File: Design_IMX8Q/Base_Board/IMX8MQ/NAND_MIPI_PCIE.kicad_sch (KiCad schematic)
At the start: 6 parts, among them U1 MIMX8MQ6CVAHZAB, U7 MT25QUxxxxxx1xW7, X1 ABLNO

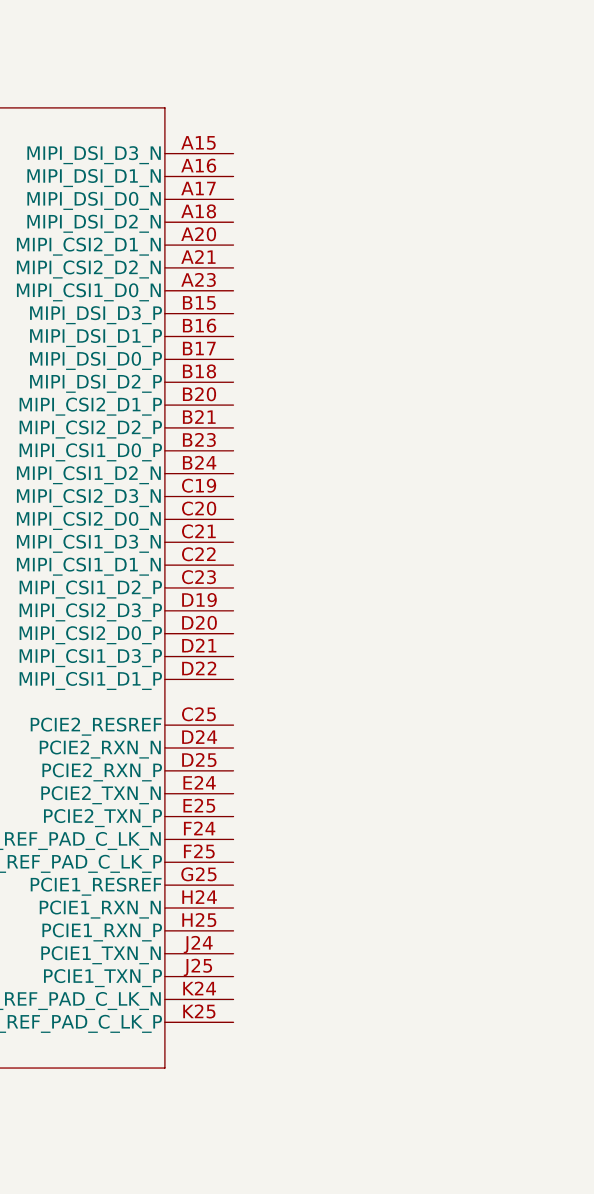
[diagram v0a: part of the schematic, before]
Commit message: Update IMX6QP and IMX8MQ
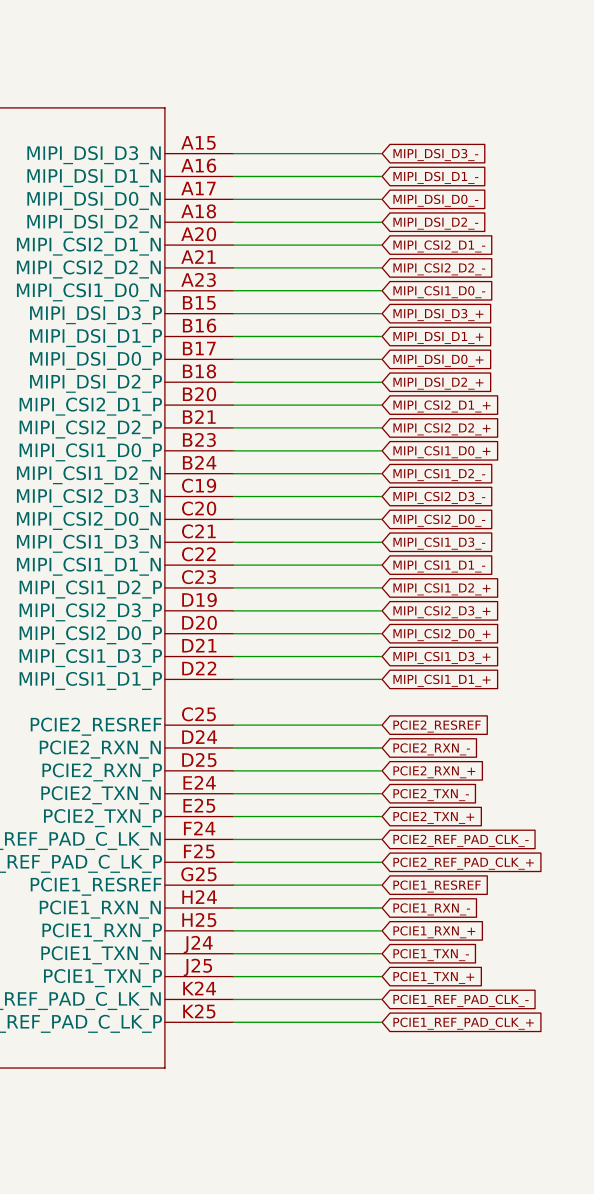
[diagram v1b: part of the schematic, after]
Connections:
- net MIPI_DSI_D3_-: now reaches U1.A15 (MIPI_DSI_D3_N)
- net MIPI_DSI_D1_-: now reaches U1.A16 (MIPI_DSI_D1_N)
- net MIPI_DSI_D0_-: now reaches U1.A17 (MIPI_DSI_D0_N)
- net MIPI_DSI_D2_-: now reaches U1.A18 (MIPI_DSI_D2_N)
- net MIPI_CSI2_D1_-: now reaches U1.A20 (MIPI_CSI2_D1_N)
- net MIPI_CSI2_D2_-: now reaches U1.A21 (MIPI_CSI2_D2_N)
- net MIPI_CSI1_D0_-: now reaches U1.A23 (MIPI_CSI1_D0_N)
- net MIPI_DSI_D3_+: now reaches U1.B15 (MIPI_DSI_D3_P)
- net MIPI_DSI_D1_+: now reaches U1.B16 (MIPI_DSI_D1_P)
- net MIPI_DSI_D0_+: now reaches U1.B17 (MIPI_DSI_D0_P)
- net MIPI_DSI_D2_+: now reaches U1.B18 (MIPI_DSI_D2_P)
- net MIPI_CSI2_D1_+: now reaches U1.B20 (MIPI_CSI2_D1_P)
- net MIPI_CSI2_D2_+: now reaches U1.B21 (MIPI_CSI2_D2_P)
- net MIPI_CSI1_D0_+: now reaches U1.B23 (MIPI_CSI1_D0_P)
- net MIPI_CSI1_D2_-: now reaches U1.B24 (MIPI_CSI1_D2_N)
- net MIPI_CSI2_D3_-: now reaches U1.C19 (MIPI_CSI2_D3_N)
- net MIPI_CSI2_D0_-: now reaches U1.C20 (MIPI_CSI2_D0_N)
- net MIPI_CSI1_D3_-: now reaches U1.C21 (MIPI_CSI1_D3_N)
- net MIPI_CSI1_D1_-: now reaches U1.C22 (MIPI_CSI1_D1_N)
- net MIPI_CSI1_D2_+: now reaches U1.C23 (MIPI_CSI1_D2_P)
- net PCIE2_RESREF: now reaches U1.C25 (PCIE2_RESREF)
- net MIPI_CSI2_D3_+: now reaches U1.D19 (MIPI_CSI2_D3_P)
- net MIPI_CSI2_D0_+: now reaches U1.D20 (MIPI_CSI2_D0_P)
- net MIPI_CSI1_D3_+: now reaches U1.D21 (MIPI_CSI1_D3_P)
- net MIPI_CSI1_D1_+: now reaches U1.D22 (MIPI_CSI1_D1_P)
- net PCIE2_RXN_-: now reaches U1.D24 (PCIE2_RXN_N)
- net PCIE2_RXN_+: now reaches U1.D25 (PCIE2_RXN_P)
- net PCIE2_TXN_-: now reaches U1.E24 (PCIE2_TXN_N)
- net PCIE2_TXN_+: now reaches U1.E25 (PCIE2_TXN_P)
- net PCIE2_REF_PAD_CLK_-: now reaches U1.F24 (PCIE2_REF_PAD_C_LK_N)
- net PCIE2_REF_PAD_CLK_+: now reaches U1.F25 (PCIE2_REF_PAD_C_LK_P)
- net PCIE1_RESREF: now reaches U1.G25 (PCIE1_RESREF)
- net PCIE1_RXN_-: now reaches U1.H24 (PCIE1_RXN_N)
- net PCIE1_RXN_+: now reaches U1.H25 (PCIE1_RXN_P)
- net PCIE1_TXN_-: now reaches U1.J24 (PCIE1_TXN_N)
- net PCIE1_TXN_+: now reaches U1.J25 (PCIE1_TXN_P)
- net PCIE1_REF_PAD_CLK_-: now reaches U1.K24 (PCIE1_REF_PAD_C_LK_N)
- net PCIE1_REF_PAD_CLK_+: now reaches U1.K25 (PCIE1_REF_PAD_C_LK_P)

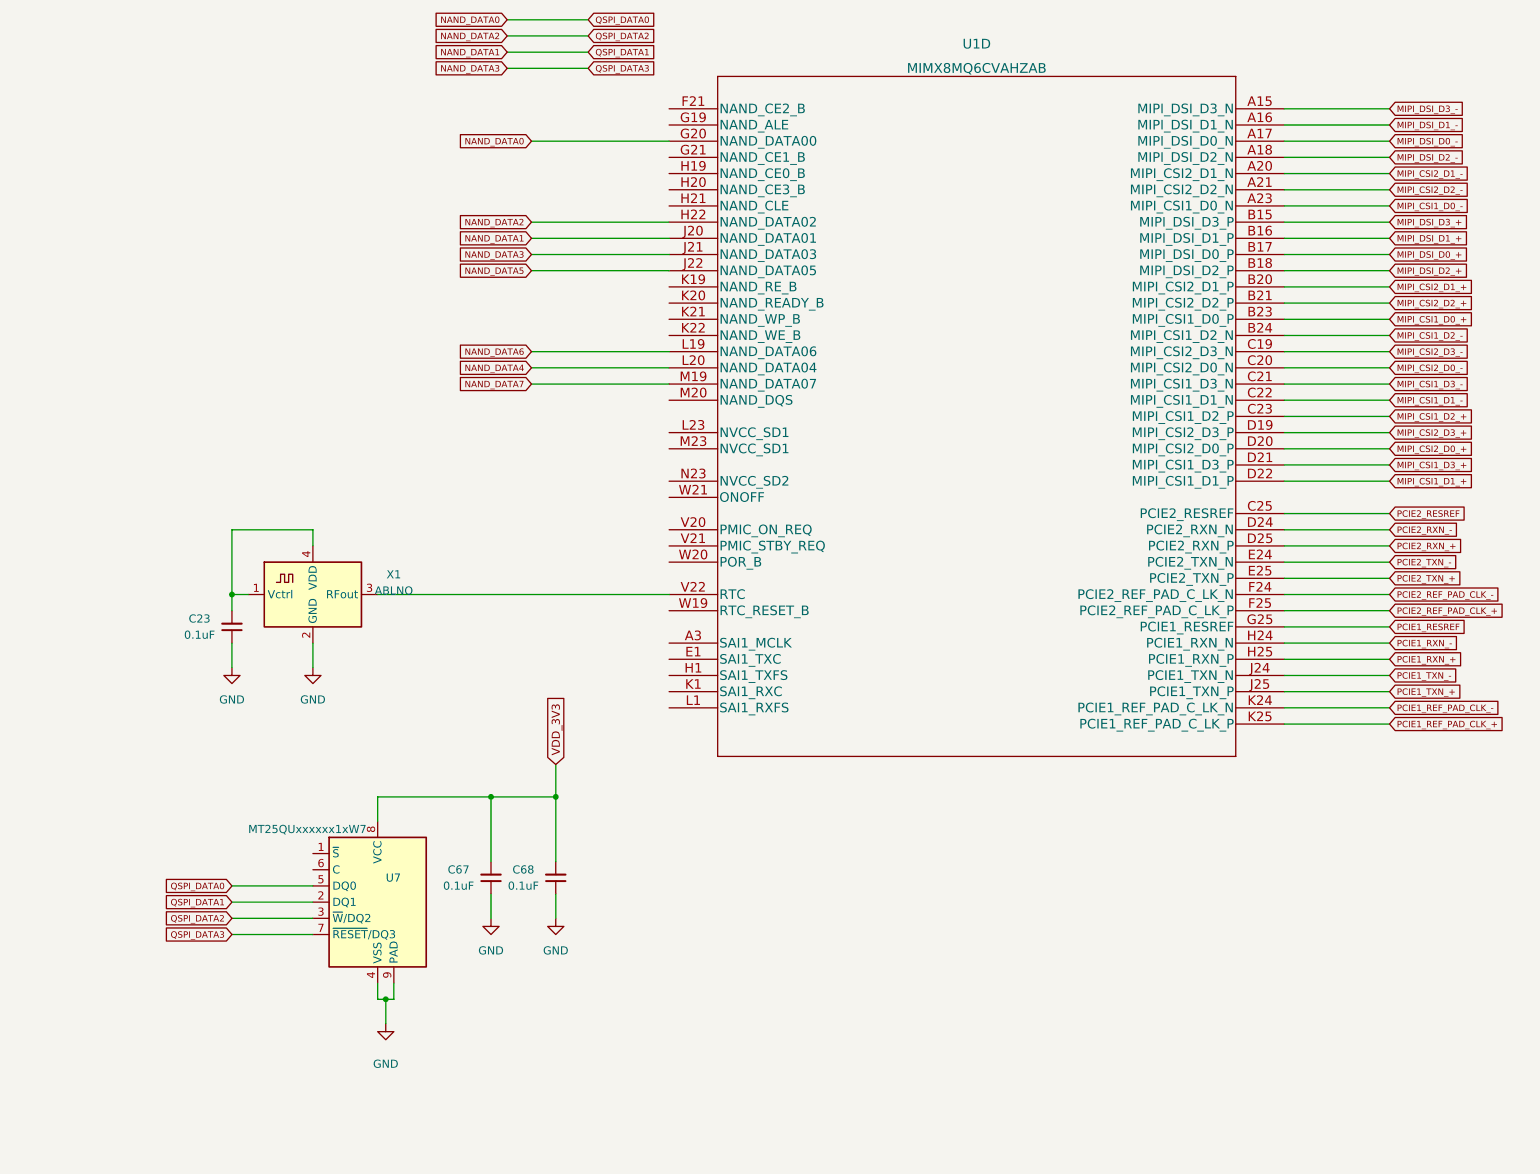
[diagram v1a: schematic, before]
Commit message: Add QSPI and more color
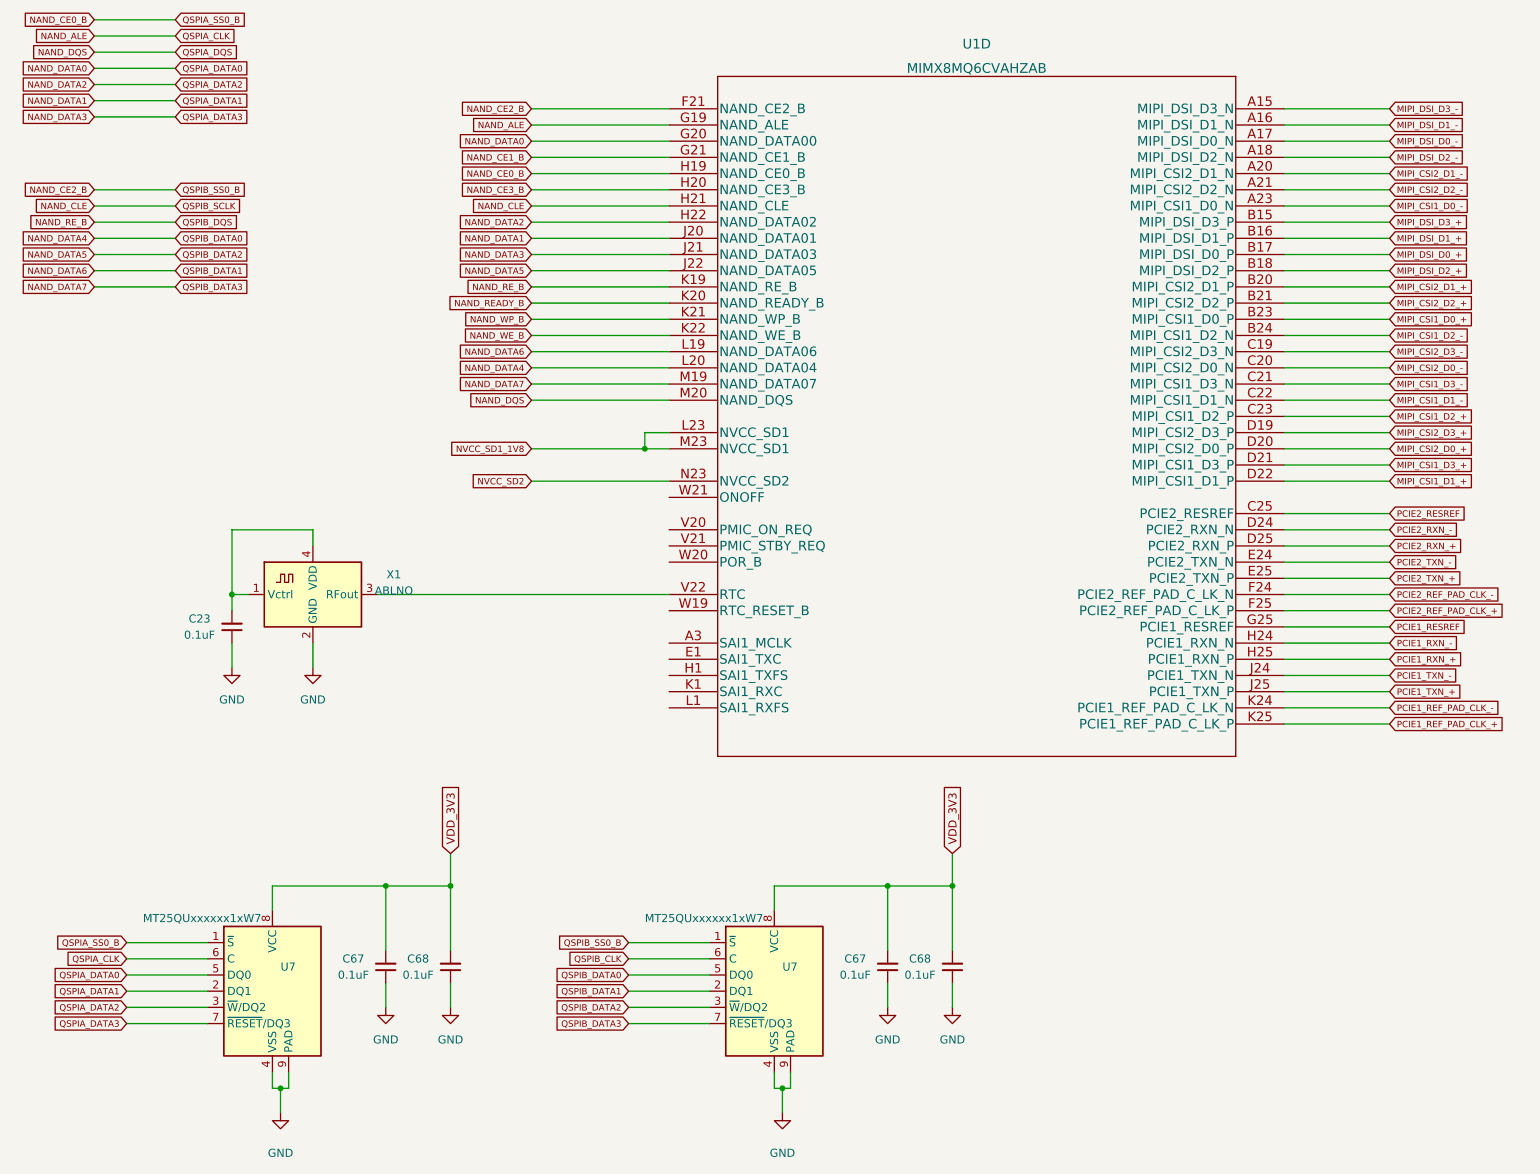
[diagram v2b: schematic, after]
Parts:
- added C67, C68: 0.1uF, Capacitor_SMD:C_0402_1005Metric, symbol Device:C_Small
- added U7: MT25QUxxxxxx1xW7, Package_DFN_QFN:W-PDFN-8-1EP_6x5mm_P1.27mm_EP3x3mm, symbol Memory_Flash:MT25QUxxxxxx1xW7
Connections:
- net GND: now also C67.1, C68.1, U7.4 (VSS), U7.9 (PAD)
- net NAND_DATA4: now also U7.5 (DQ0)
- net NAND_DATA5: now also U7.3 (~{W}/DQ2)
- net NAND_DATA6: now also U7.2 (DQ1)
- net NAND_DATA7: now also U7.7 (~{RESET}/DQ3)
- net VDD_3V3: now also C67.2, C68.2, U7.8 (VCC)
- net NAND_CE0_B: now reaches U7.1 (~{S})
- net NAND_CE0_B: now also U1.H19 (NAND_CE0_B)
- net NAND_ALE: now reaches U7.6 (C)
- net NAND_ALE: now also U1.G19 (NAND_ALE)
- net NAND_CE2_B: now reaches U1.F21 (NAND_CE2_B)
- net NAND_CE2_B: now also U7.1 (~{S})
- net NAND_CE1_B: now reaches U1.G21 (NAND_CE1_B)
- net NAND_CE3_B: now reaches U1.H20 (NAND_CE3_B)
- net NAND_CLE: now reaches U1.H21 (NAND_CLE)
- net NAND_RE_B: now reaches U1.K19 (NAND_RE_B)
- net NAND_READY_B: now reaches U1.K20 (NAND_READY_B)
- net NAND_WP_B: now reaches U1.K21 (NAND_WP_B)
- net NAND_WE_B: now reaches U1.K22 (NAND_WE_B)
- net NVCC_SD1_1V8: now reaches U1.L23 (NVCC_SD1)
- net NVCC_SD1_1V8: now also U1.M23 (NVCC_SD1)
- net NAND_DQS: now reaches U1.M20 (NAND_DQS)
- net NVCC_SD2: now reaches U1.N23 (NVCC_SD2)
- new net QSPIB_CLK: U7.6 (C)
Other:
- moved on the sheet: C67, C68, U7

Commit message: it was inserted power control system
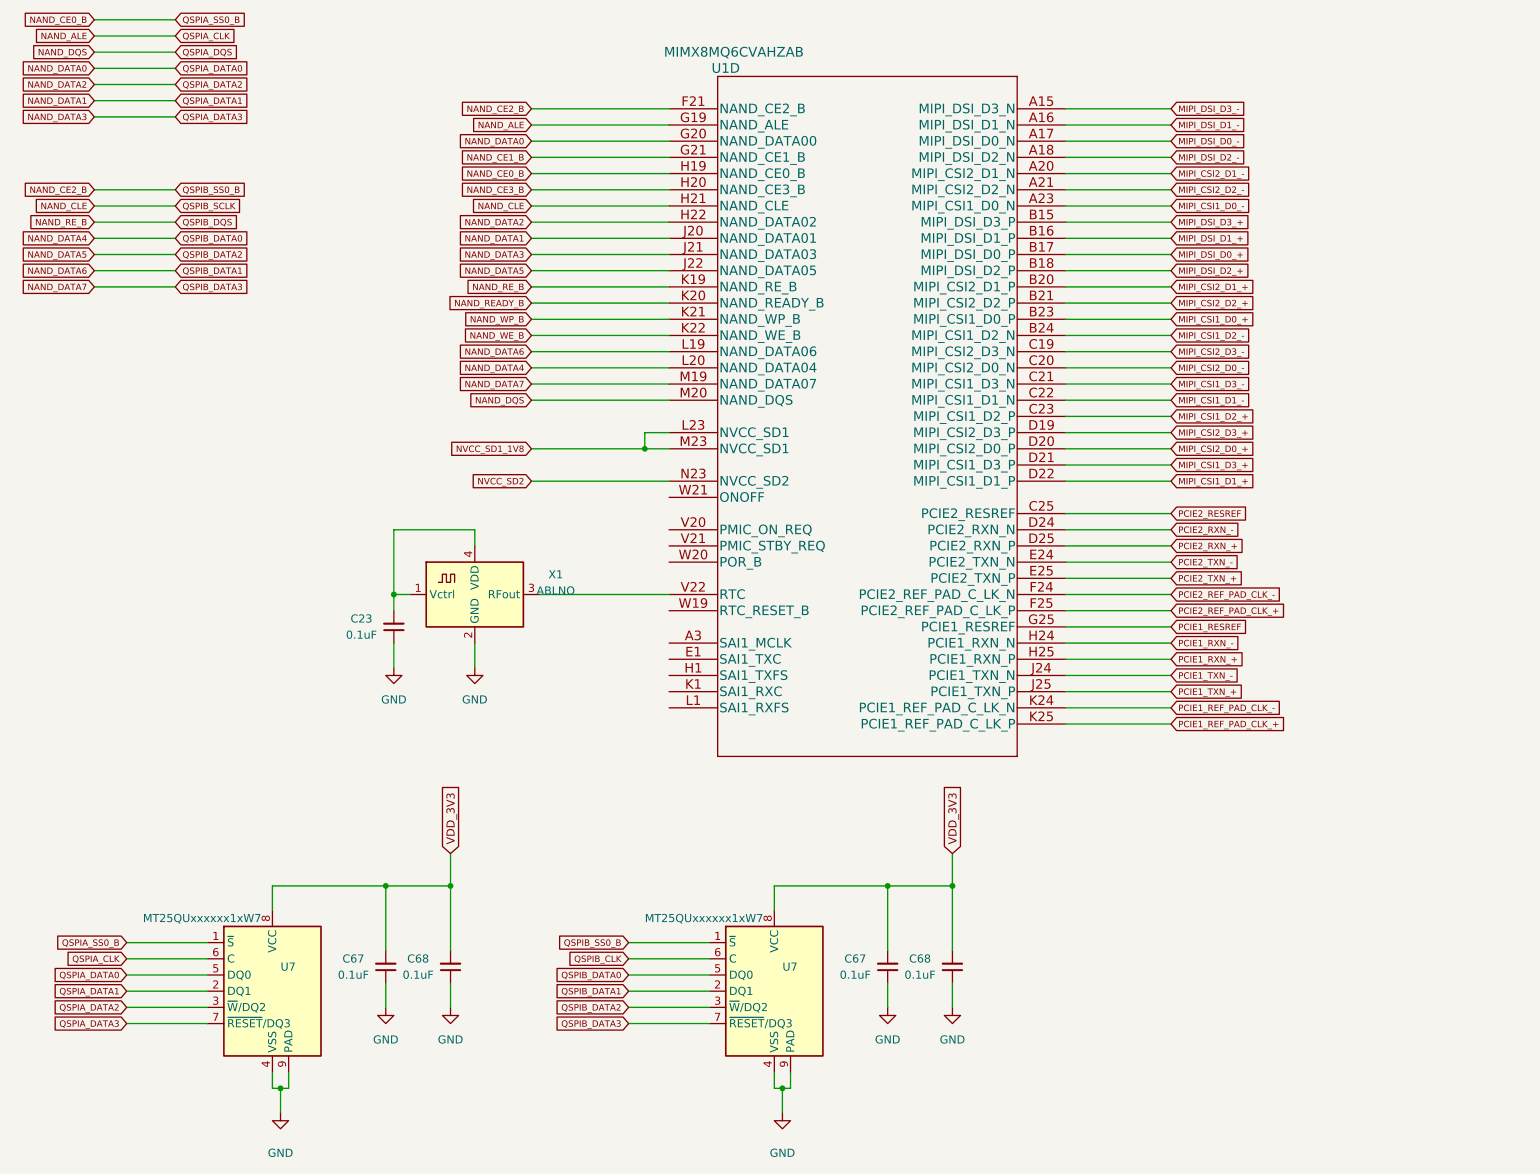
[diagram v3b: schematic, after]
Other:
- moved on the sheet: C23, U1D, X1
